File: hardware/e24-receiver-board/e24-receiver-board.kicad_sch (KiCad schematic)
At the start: 21 parts, among them J1 505070-2422, J10 SPEAKER-, J11 GND1, J12 TRACK_RIGHT, J13 MOTOR+, J14 LAMP_REAR, J15 CAP+, J16 U+, J17 AUX3, J18 AUX10, J19 AUX12, J2 TRACK_LEFT, J20 SPEAKER+, J21 GND2, J3 MOTOR-, J4 LAMP_FRONT, J5 VCC, J6 AUX1, J7 AUX2, J8 AUX4, J9 AUX11

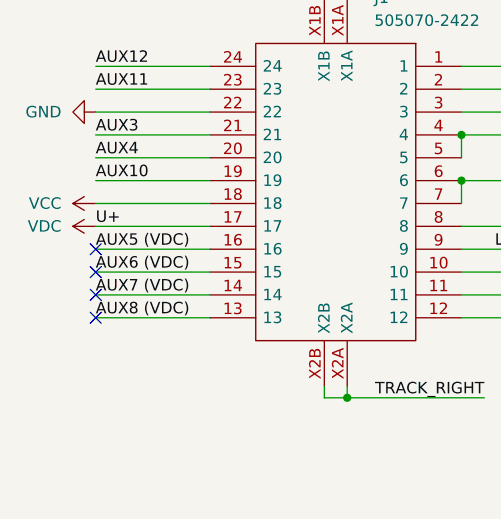
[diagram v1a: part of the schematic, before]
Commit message: fix: update to kicad 9.0
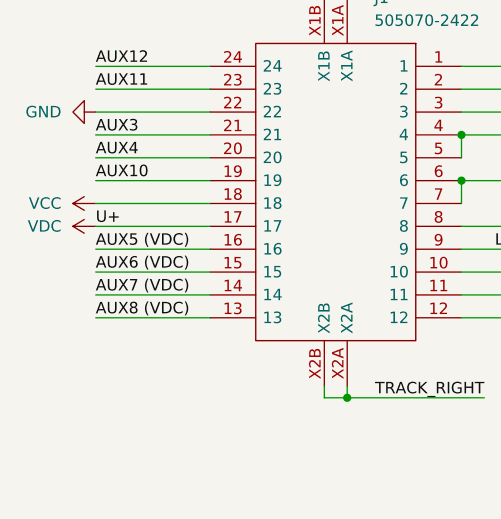
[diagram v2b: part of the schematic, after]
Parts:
- J1: footprint 5050702422 -> e24-receiver-board:CONN-SMD_24P-P0.35_5050702422; symbol Local Symbol Library:505070-2422 -> e24-receiver-board:505070-2422; Description_1 SlimStack Board-to-Board Connector, 0.35mm Pitch, SSB RP Se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 -> (none)
- J10, J14, J15, J16, J17, J18, J19, J20, J4, J5, J6, J7, J8, J9: footprint Connector_Wire:SolderWirePad_1x01_SMD_1x2mm -> e24-receiver-board:SolderWirePad_1x01_SMD_1x2mm; symbol Connector_Generic:Conn_01x01 -> e24-receiver-board:Conn_01x01
- J11, J12, J13, J2, J21, J3: footprint Local Library:SolderWirePad_1x01_SMD_1.5x3mm -> e24-receiver-board:SolderWirePad_1x01_SMD_1.5x3mm; symbol Connector_Generic:Conn_01x01 -> e24-receiver-board:Conn_01x01
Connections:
- no-connect marks 4 -> 0
